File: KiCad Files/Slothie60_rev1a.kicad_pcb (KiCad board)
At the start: 2 copper layers, 285 x 94.6 mm, 160 parts, among them SW1 SW_Push, SW10 SW_Push, SW11 SW_Push, SW12 SW_Push, SW13 SW_Push, SW14 SW_Push, SW15 SW_Push, SW16 SW_Push, SW17 SW_Push, SW18 SW_Push, SW19 SW_Push, SW2 SW_Push, SW20 SW_Push, SW21 SW_Push, SW22 SW_Push, SW23 SW_Push, SW24 SW_Push, SW25 SW_Push, SW26 SW_Push, SW27 SW_Push, SW28 SW_Push, SW29 SW_Push, SW3 SW_Push, SW30 SW_Push, SW31 SW_Push, SW32 SW_Push, SW33 SW_Push, SW34 SW_Push, SW35 SW_Push, SW36 SW_Push, SW37 SW_Push, SW38 SW_Push, SW39 SW_Push, SW4 SW_Push, SW40 SW_Push, SW41 SW_Push, SW42 SW_Push, SW43 SW_Push, SW44 SW_Push, SW45 SW_Push, SW46 SW_Push, SW47 SW_Push, SW48 SW_Push, SW49 SW_Push, SW5 SW_Push, SW50 SW_Push, SW51 SW_Push, SW52 SW_Push, SW53 SW_Push, SW54 SW_Push, SW55 SW_Push, SW56 SW_Push, SW57 SW_Push, SW58 SW_Push, SW59 SW_Push, SW6 SW_Push, SW60 SW_Push, SW61 SW_Push, SW62 SW_Push, SW63 SW_Push, SW64 SW_Push, SW65 SW_Push, SW66 SW_Push, SW67 SW_Push, SW68 SW_Push, SW7 SW_Push, SW8 SW_Push, SW9 SW_Push

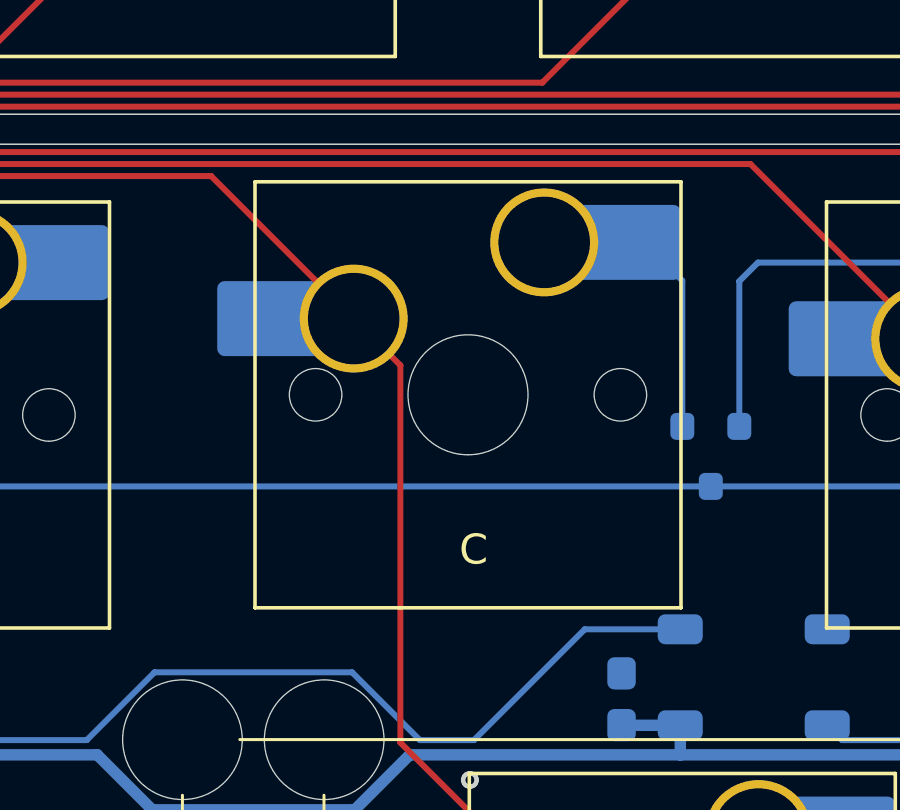
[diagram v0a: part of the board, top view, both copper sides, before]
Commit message: Update
KiCad files had one small error, fixed it now
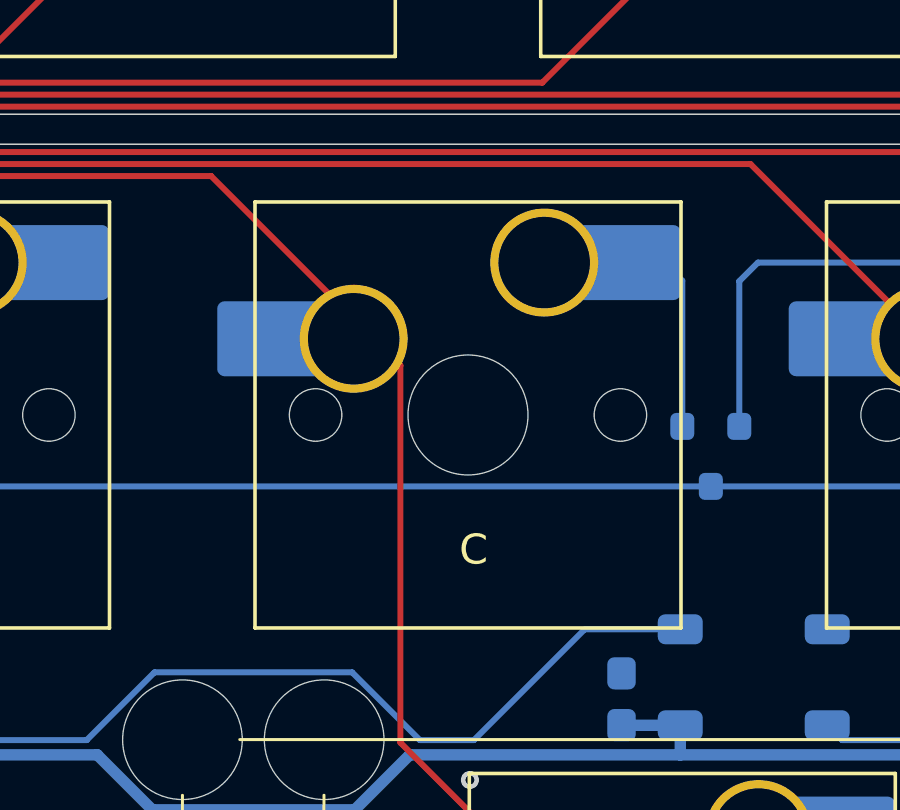
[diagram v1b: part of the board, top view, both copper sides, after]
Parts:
- moved SW47 0.67 mm to (186.1, 157.5)
